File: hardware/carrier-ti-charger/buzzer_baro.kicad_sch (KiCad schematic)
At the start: 25 parts, among them J12 CONTROLS, SW2 K3-1280S-F1, SW3 K3-1280S-F1, U10 BMP580, U13 TCA9534PWR, U9 SN74LVC1G17DBVR

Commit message: Polishing.
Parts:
- renumbered J12 to J10
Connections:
- net GND: no longer U10.7 (INT)
- no-connect marks 6 -> 7

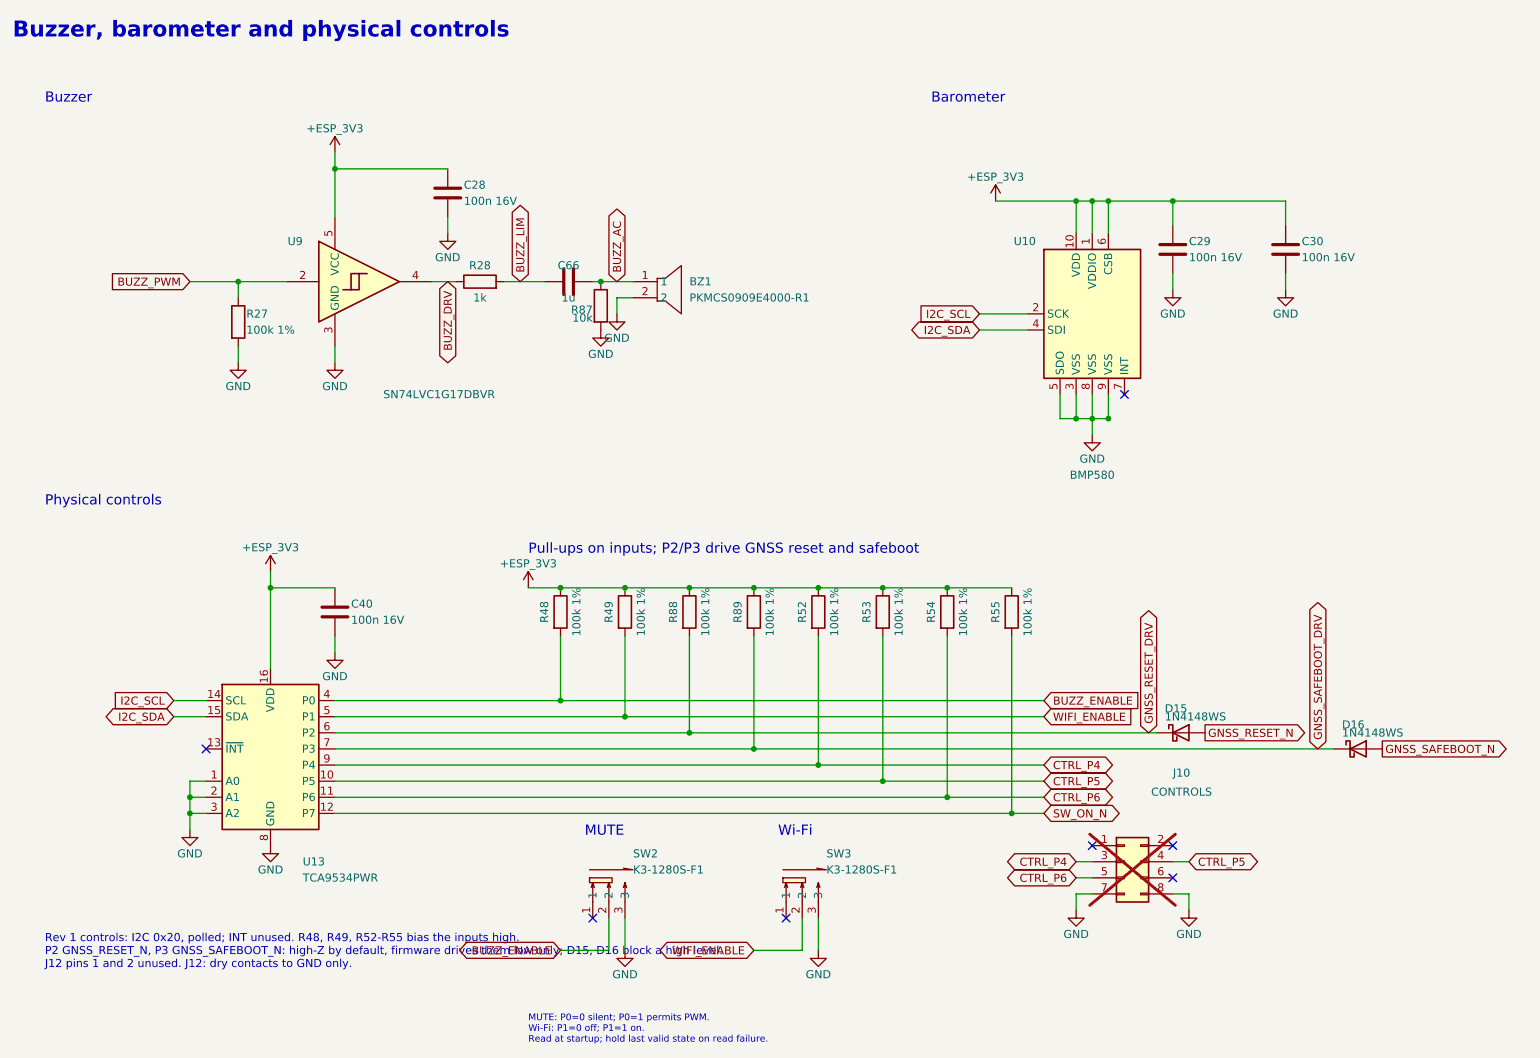
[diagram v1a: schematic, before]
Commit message: Consolidate BOM, add GNSS listen to ESP.
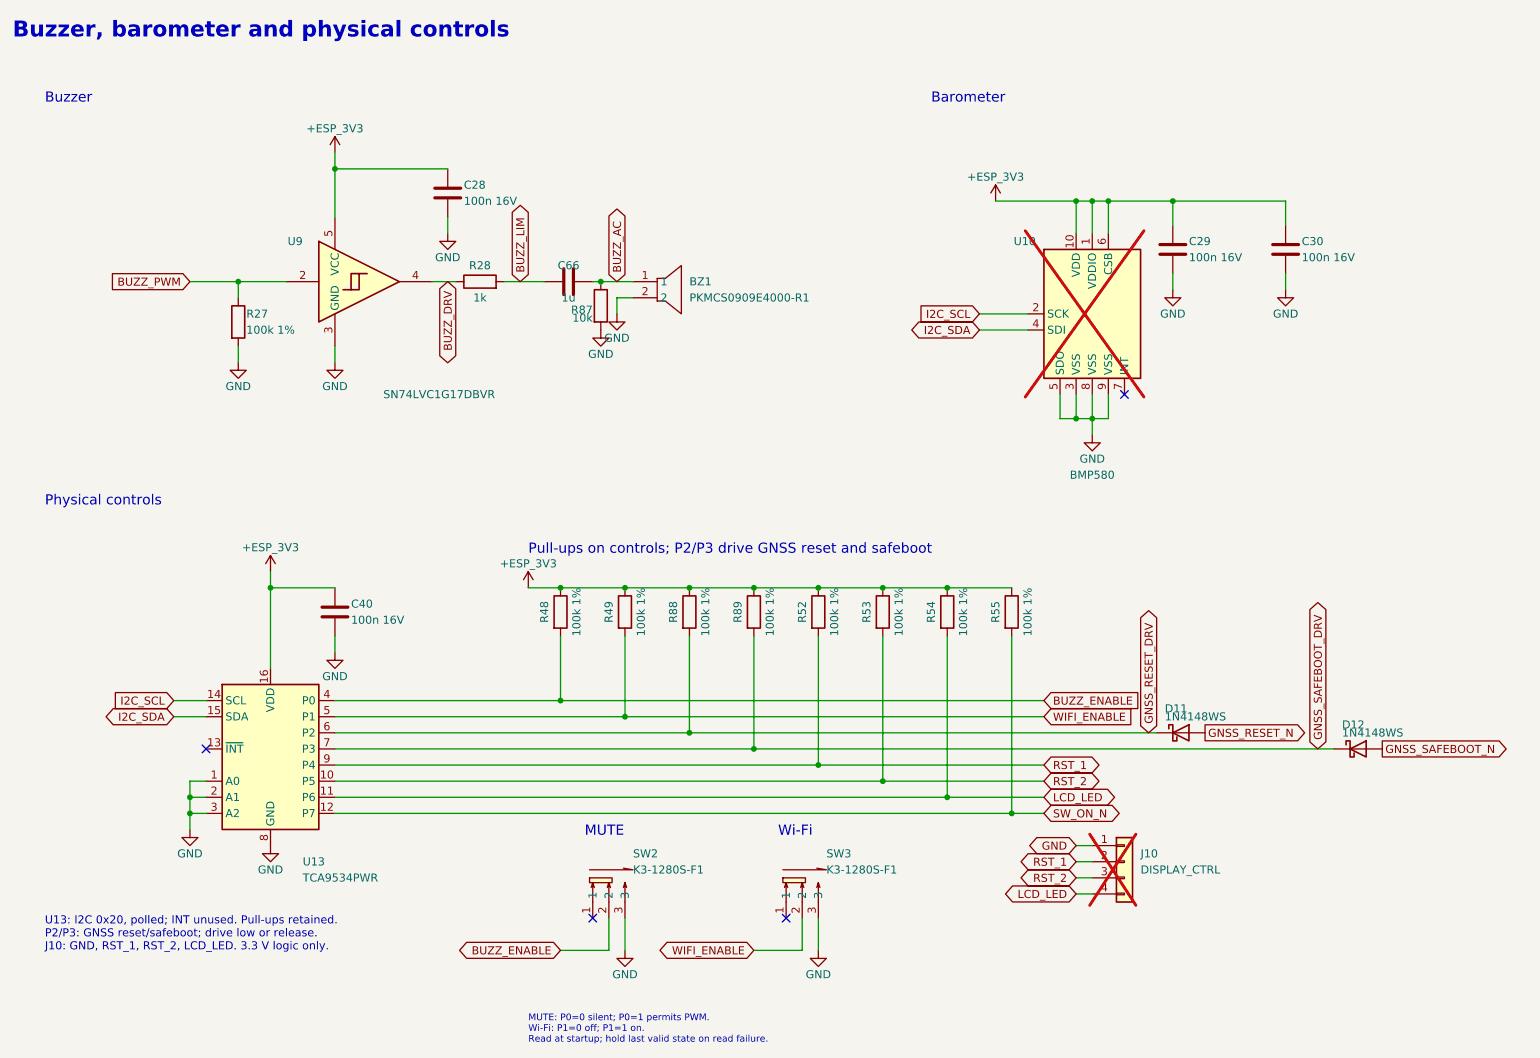
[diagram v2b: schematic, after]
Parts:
- BZ1: footprint carrier:BUZ-SMD_L9.0-W9.0_PKMCS0909E4000-R1 -> Mark:BUZ-SMD_L9.0-W9.0_PKMCS0909E4000-R1; symbol carrier:PKMCS0909E4000-R1 -> Mark:PKMCS0909E4000-R1
- C28, C29, C30, C40: footprint carrier:C_0402_1005Metric_NoSilk -> Mark:C_0402_1005Metric_NoSilk
- J10: value CONTROLS -> DISPLAY_CTRL; footprint Connector_PinHeader_2.54mm:PinHeader_2x04_P2.54mm_Vertical -> Connector_PinHeader_2.54mm:PinHeader_1x04_P2.54mm_Vertical; symbol Connector_Generic:Conn_02x04_Odd_Even -> Connector_Generic:Conn_01x04
- R87: footprint carrier:R_0402_1005Metric_NoSilk -> Mark:R_0402_1005Metric_NoSilk
- SW2, SW3: footprint carrier:SW-SMD_K3-1280S-F1 -> Mark:SW-SMD_K3-1280S-F1; symbol carrier:K3-1280S-F1 -> Mark:K3-1280S-F1
- U10: footprint carrier:LGA-10_L2.0-W2.0-P0.50-TL_BMP581 -> Mark:LGA-10_L2.0-W2.0-P0.50-TL_BMP581; symbol carrier:BMP581 -> Mark:BMP581; now not fitted; now left out of the parts list
- renumbered D15 to D11, D16 to D12
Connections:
- net GND: now also J10.1 (Pin_1); no longer J10.7 (Pin_7), J10.8 (Pin_8)
- net RST_1: now reaches J10.2 (Pin_2)
- net RST_1: now also R52.2, U13.9 (P4)
- removed net CTRL_P4: J10.3 (Pin_3), R52.2, U13.9 (P4)
- net CTRL_P5 renamed RST_2
- net RST_2: now also J10.3 (Pin_3); no longer J10.4 (Pin_4)
- net CTRL_P6 renamed LCD_LED
- net LCD_LED: now also J10.4 (Pin_4); no longer J10.5 (Pin_5)
- no-connect marks 7 -> 4
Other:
- note added: "Pull-ups on controls; P2/P3 drive GNSS reset and safeboot"
- note added: "U13: I2C 0x20, polled; INT unused. Pull-ups retained. P2/P3: GNSS reset/safeboot; drive low or release. J10: GND, RST_1, RST_2, LCD_LED. 3.3 V logic only."
- note removed: "Pull-ups on inputs; P2/P3 drive GNSS reset and safeboot"
- note removed: "Rev 1 controls: I2C 0x20, polled; INT unused. R48, R49, R52-R55 bias the inputs high. P2 GNSS_RESET_N, P3 GNSS_SAFEBOOT_N: high-Z by default, firmware drives them low only; D15, D16 block a high level. J12 pins 1 and 2 unused. J12: dry contacts to GND only."

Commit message: Order revision A.
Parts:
- U10: now fitted; now in the parts list
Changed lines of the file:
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@@
 		(body_style 1)
 		(exclude_from_sim no)
-		(in_bom no)
+		(in_bom yes)
 		(on_board yes)
-		(in_pos_files no)
-		(dnp yes)
+		(in_pos_files yes)
+		(dnp no)
 		(property "Reference" "U10"
 			(at 181.61 54.61 0)
